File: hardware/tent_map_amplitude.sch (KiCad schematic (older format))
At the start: 1 part

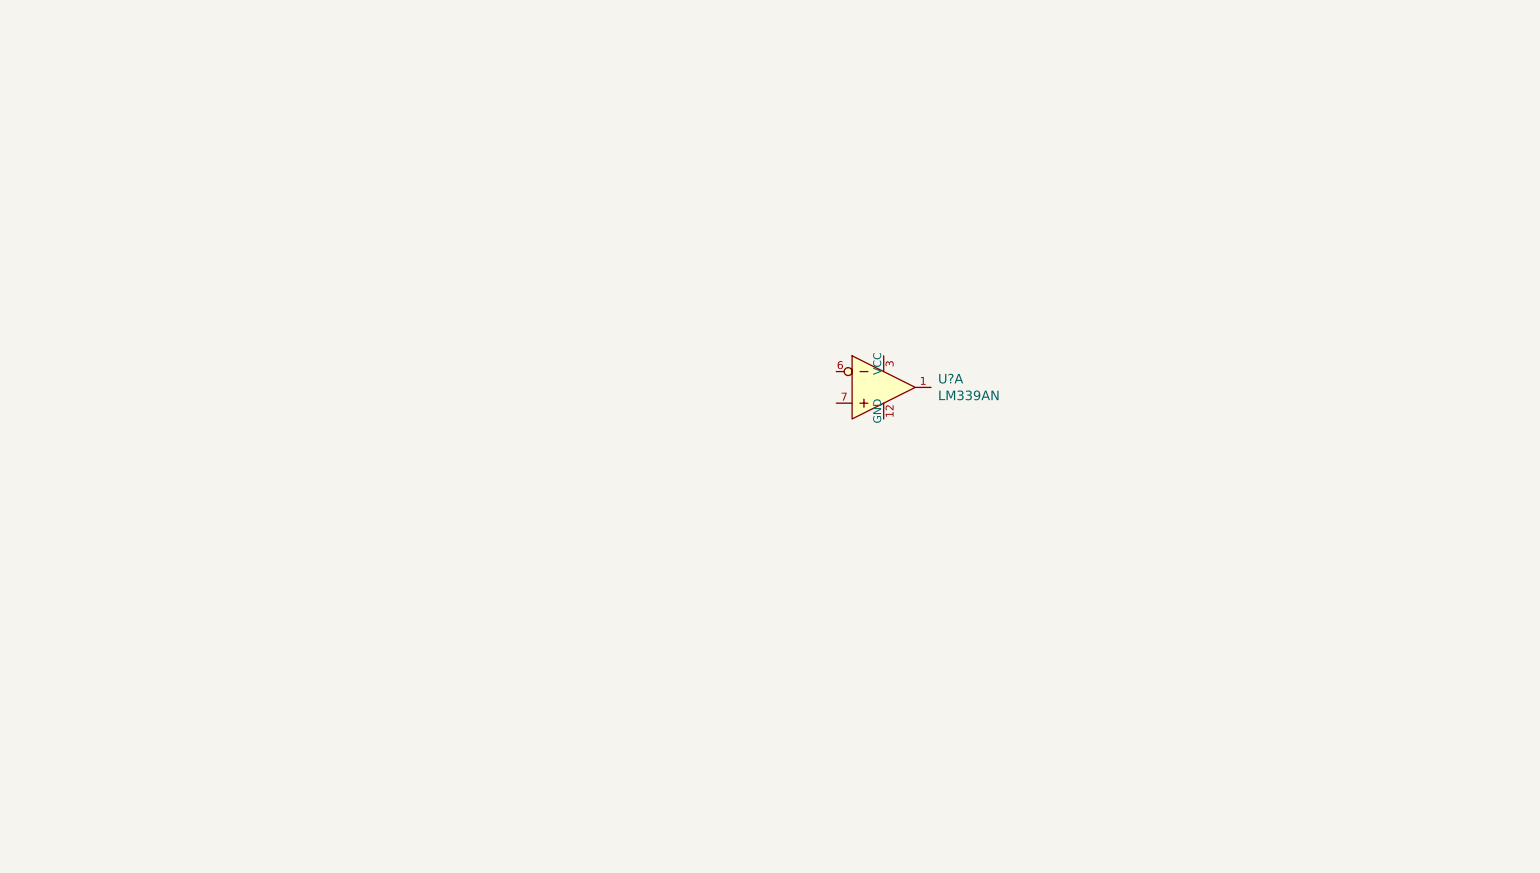
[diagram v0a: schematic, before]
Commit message: Add basic circuit schematic
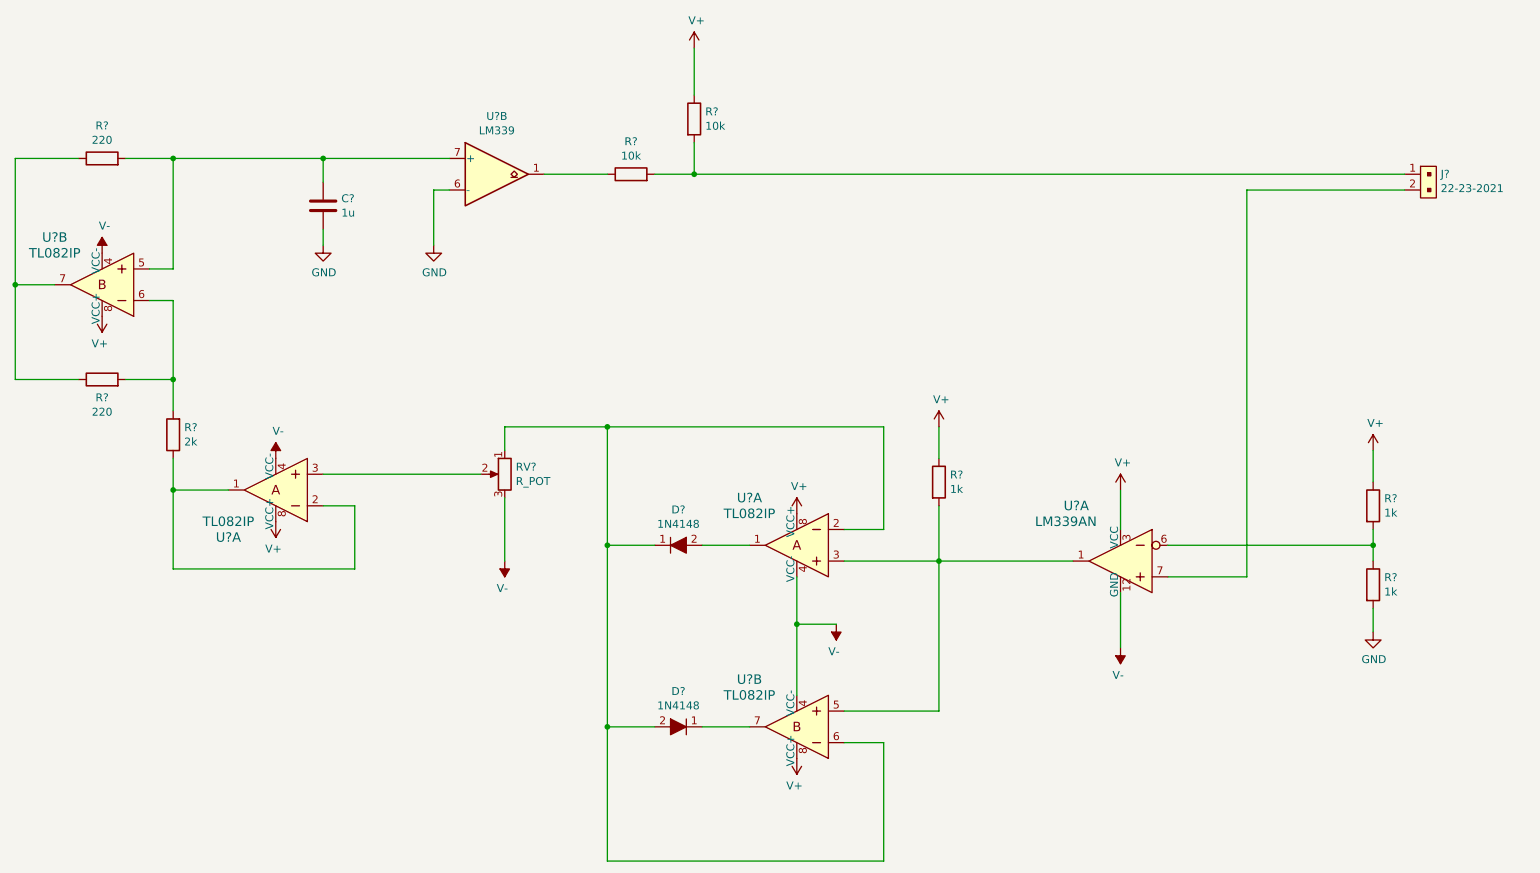
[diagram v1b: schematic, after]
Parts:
- added C?: 1u, symbol Device:C
- added D? (x2): 1N4148, digikey-footprints:Diode_DO-35_P10mm, symbol dk_Diodes-Rectifiers-Single:1N4148
- added J?: 22-23-2021, digikey-footprints:PinHeader_1x2_P2.54mm_Drill1.02mm, symbol dk_Rectangular-Connectors-Headers-Male-Pins:22-23-2021
- added R? (x3): 1k, symbol Device:R
- added R?: 2k, symbol Device:R
- added R? (x2): 220, symbol Device:R
- added R? (x2): 10k, symbol Device:R
- added RV?: R_POT, symbol Device:R_POT
- added U? (x4): TL082IP, digikey-footprints:DIP-8_W7.62mm, symbol dk_Linear-Amplifiers-Instrumentation-OP-Amps-Buffer-Amps:TL082IP
- added U?: LM339, symbol Comparator:LM339
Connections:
- net at U?.1: now also R?.2, U?.3, U?.5
- net V-: now reaches U?.12 (GND)
- net V-: now also RV?.3, U?.4 (VCC-), U?.4 (VCC-), U?.4 (VCC-), U?.4 (VCC-)
- net V+: now reaches U?.3 (VCC)
- net V+: now also R?.1, R?.1, R?.1, U?.8 (VCC+), U?.8 (VCC+), U?.8 (VCC+), U?.8 (VCC+)
- net at U?.6: now also R?.1, R?.2
- net at U?.7: now also J?.2
- new net: D?.2, U?.1
- new net: D?.1, D?.2, RV?.1, U?.2, U?.6
- new net: D?.1, U?.7
- new net: R?.1, U?.1, U?.2
- new net: RV?.2, U?.3
- new net: C?.1, R?.2, U?.5, U?.7 (+)
- new net: R?.2, R?.2, U?.6
- new net: R?.1, R?.1, U?.7
- new net: R?.1, U?.1
- new net: J?.1, R?.2, R?.2
- new net GND: C?.2, R?.2, U?.6 (-)
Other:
- moved on the sheet: U?A

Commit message: Add decoupling capacitors
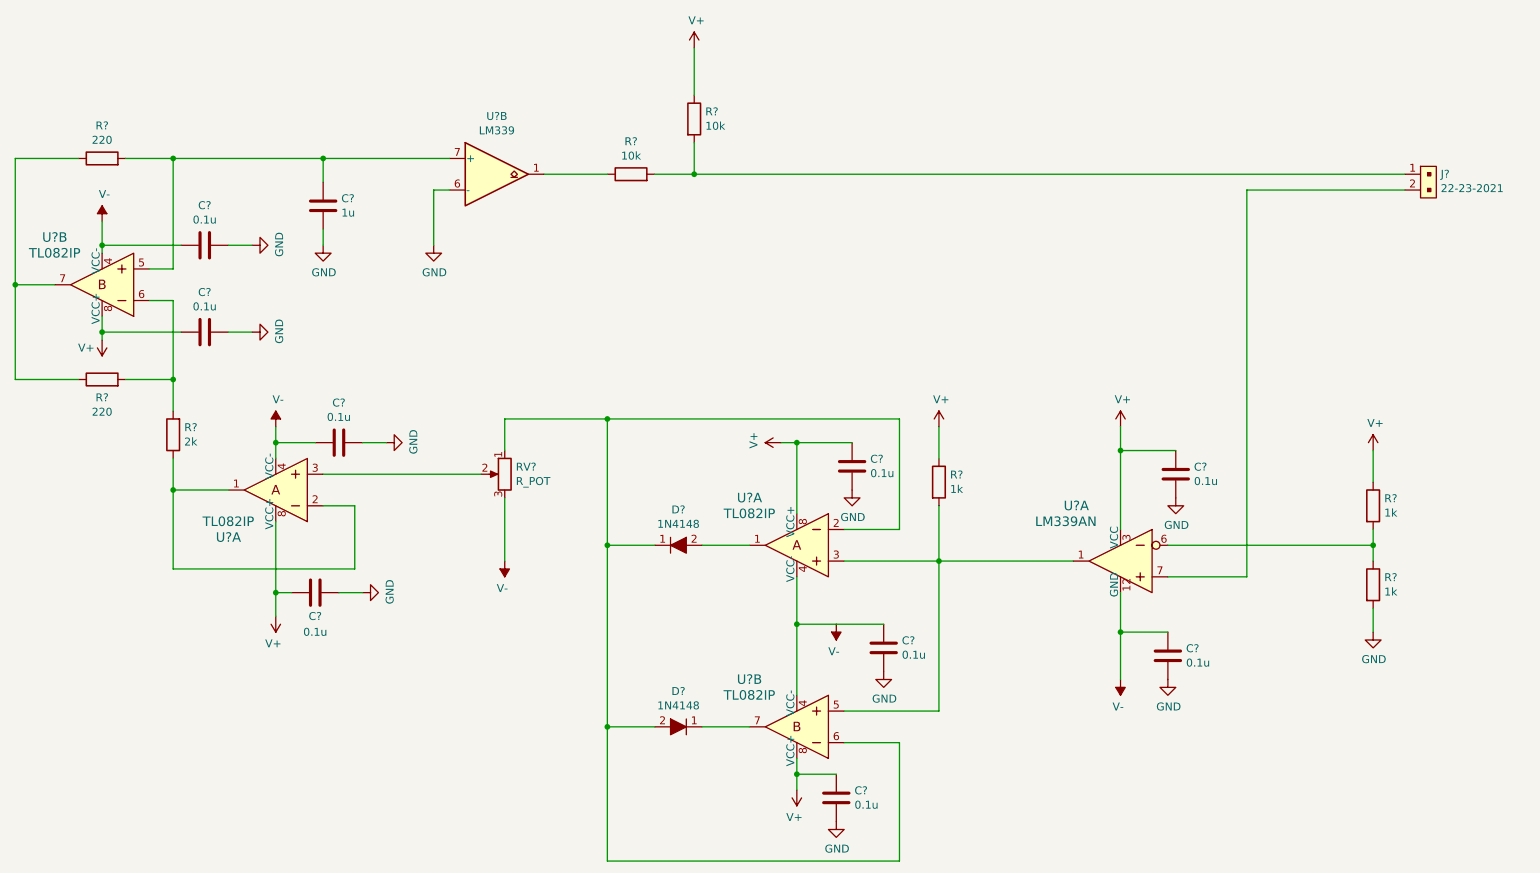
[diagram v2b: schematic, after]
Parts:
- added C? (x9): 0.1u, symbol Device:C
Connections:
- net GND: now also C?.1, C?.1, C?.1, C?.1, C?.2, C?.2, C?.2, C?.2, C?.2
- net V+: now also C?.1, C?.1, C?.1, C?.2, C?.2
- net V-: now also C?.1, C?.1, C?.2, C?.2

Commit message: Remove extra capacitors, only need 2 for each IC package
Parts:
- removed C? (x3): 0.1u, symbol Device:C
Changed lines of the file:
@@
 Wire Wire Line
 	6500 5150 6200 5150
-$Comp
-L Device:C C?
-U 1 1 5FA678DE
-P 6300 4150
-F 0 "C?" H 6415 4196 50  0000 L CNN
-F 1 "0.1u" H 6415 4105 50  0000 L CNN
-F 2 "" H 6338 4000 50  0001 C CNN
-F 3 "~" H 6300 4150 50  0001 C CNN
-	1    6300 4150
-	1    0    0    -1
-$EndComp
-$Comp
-L power:GND #PWR?
-U 1 1 5FA678E4
-P 6300 4300
-F 0 "#PWR?" H 6300 4050 50  0001 C CNN
-F 1 "GND" H 6305 4127 50  0000 C CNN
-F 2 "" H 6300 4300 50  0001 C CNN
-F 3 "" H 6300 4300 50  0001 C CNN
-	1    6300 4300
-	1    0    0    -1
-$EndComp
 Connection ~ 4750 3850
 Wire Wire Line
@@
 Wire Wire Line
 	5850 4000 5950 4000
-Connection ~ 5950 4000
 Wire Wire Line
 	5950 4000 5950 4450
-Wire Wire Line
-	5950 4000 6300 4000
 $Comp
 L Device:C C?
@@
 	2650 4500 2650 4950
 Connection ~ 2650 4950
-$Comp
-L Device:C C?
-U 1 1 5FADDE83
-P 2200 2750
-F 0 "C?" V 1948 2750 50  0000 C CNN
-F 1 "0.1u" V 2039 2750 50  0000 C CNN
-F 2 "" H 2238 2600 50  0001 C CNN
-F 3 "~" H 2200 2750 50  0001 C CNN
-	1    2200 2750
-	0    1    1    0
-$EndComp
-$Comp
-L power:GND #PWR?
-U 1 1 5FADDE89
-P 2500 2750
-F 0 "#PWR?" H 2500 2500 50  0001 C CNN
-F 1 "GND" H 2505 2577 50  0000 C CNN
-F 2 "" H 2500 2750 50  0001 C CNN
-F 3 "" H 2500 2750 50  0001 C CNN
-	1    2500 2750
-	0    -1   -1   0
-$EndComp
 Wire Wire Line
-	2500 2750 2350 2750
-$Comp
-L Device:C C?
-U 1 1 5FAE0791
-P 2200 3300
-F 0 "C?" V 1948 3300 50  0000 C CNN
-F 1 "0.1u" V 2039 3300 50  0000 C CNN
-F 2 "" H 2238 3150 50  0001 C CNN
-F 3 "~" H 2200 3300 50  0001 C CNN
-	1    2200 3300
-	0    1    1    0
-$EndComp
-$Comp
-L power:GND #PWR?
-U 1 1 5FAE0797
-P 2500 3300
-F 0 "#PWR?" H 2500 3050 50  0001 C CNN
-F 1 "GND" H 2505 3127 50  0000 C CNN
-F 2 "" H 2500 3300 50  0001 C CNN
-F 3 "" H 2500 3300 50  0001 C CNN
-	1    2500 3300
-	0    -1   -1   0
-$EndComp
+	1550 2600 1550 2800
 Wire Wire Line
-	2500 3300 2350 3300
-Wire Wire Line
-	2050 2750 1550 2750
-Wire Wire Line
-	1550 2750 1550 2600
-Wire Wire Line
-	1550 2800 1550 2750
-Connection ~ 1550 2750
-Wire Wire Line
-	2050 3300 1550 3300
-Wire Wire Line
-	1550 3300 1550 3200
-Wire Wire Line
-	1550 3350 1550 3300
-Connection ~ 1550 3300
+	1550 3200 1550 3350
 $EndSCHEMATC
